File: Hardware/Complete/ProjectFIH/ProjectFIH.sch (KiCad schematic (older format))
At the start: 22 parts, among them J1 Conn_01x02_Male, J2 Heater, Q1 2N7002, Q2 2N7002, Q3 IRLZ44N, U1 LM158

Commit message: Added 24 -> 5 regulator
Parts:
- removed J1: Conn_01x02_Male, symbol Connector:Conn_01x02_Male
- added C?: 1000uF x 48V, symbol Device:CP
- added C? (x2): 2.2uF, symbol Device:C
- added C?: 10nF, symbol Device:C
- added C?: 1000uF x 10V, symbol Device:CP
- added D?: 10BQ060, symbol Device:D_Schottky
- added L?: 27uH 1A, symbol Device:L
- added U?: LM22675-5.0, symbol Fossa_library:LM22675-5.0
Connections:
- net +24V: now also C?.1, C?.1, U?.7 (Vin)
- net +5V: now also C?.1, C?.1, L?.2, U?.4 (FB)
- net GND: now also C?.2, C?.2, C?.2, C?.2, D?.2 (A), U?.6 (GND)
- new net: C?.1, D?.1 (K), L?.1, U?.8 (SW)
- new net: C?.2, U?.1 (Boot)
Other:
- note added: "Internal needs +5V regulator"
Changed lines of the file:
@@
 Wire Wire Line
 	900  1250 900  1500
-$Comp
-L Connector:Conn_01x02_Male J1
-U 1 1 5EFE5C5A
-P 1900 1100
-F 0 "J1" H 1962 1144 50  0000 L CNN
-F 1 "Conn_01x02_Male" H 1650 900 50  0000 L CNN
-F 2 "" H 1900 1100 50  0001 C CNN
-F 3 "~" H 1900 1100 50  0001 C CNN
-	1    1900 1100
-	-1   0    0    1
-$EndComp
 Wire Wire Line
 	1200 1500 1200 1400
-$Comp
-L power:GND #PWR011
-U 1 1 5EFEE96F
-P 1650 1150
-F 0 "#PWR011" H 1650 900 50  0001 C CNN
-F 1 "GND" H 1655 977 50  0000 C CNN
-F 2 "" H 1650 1150 50  0001 C CNN
-F 3 "" H 1650 1150 50  0001 C CNN
-	1    1650 1150
-	1    0    0    -1
-$EndComp
-$Comp
-L power:+5V #PWR010
-U 1 1 5EFEF193
-P 1650 950
-F 0 "#PWR010" H 1650 800 50  0001 C CNN
-F 1 "+5V" H 1665 1123 50  0000 C CNN
-F 2 "" H 1650 950 50  0001 C CNN
-F 3 "" H 1650 950 50  0001 C CNN
-	1    1650 950
-	1    0    0    -1
-$EndComp
-Wire Wire Line
-	1650 950  1650 1000
-Wire Wire Line
-	1650 1000 1700 1000
-Wire Wire Line
-	1700 1100 1650 1100
-Wire Wire Line
-	1650 1100 1650 1150
 Text Notes 2450 2000 0    50   ~ 0
 Uout = Uin * (1 + R3/R2 + R3/R1) - Vcc * R3/R1
@@
 Wire Wire Line
 	7600 2150 7600 2350
+$Comp
+L Device:CP C?
+U 1 1 5F0A2BBD
+P 8300 1350
+F 0 "C?" H 8300 1450 50  0000 L CNN
+F 1 "1000uF x 48V" H 8000 1250 50  0000 L CNN
+F 2 "" H 8338 1200 50  0001 C CNN
+F 3 "~" H 8300 1350 50  0001 C CNN
+	1    8300 1350
+	1    0    0    -1
+$EndComp
+$Comp
+L Device:C C?
+U 1 1 5F0A57D0
+P 8650 1350
+F 0 "C?" H 8650 1450 50  0000 L CNN
+F 1 "2.2uF" H 8600 1250 50  0000 L CNN
+F 2 "" H 8688 1200 50  0001 C CNN
+F 3 "~" H 8650 1350 50  0001 C CNN
+	1    8650 1350
+	1    0    0    -1
+$EndComp
+$Comp
+L Device:C C?
+U 1 1 5F0A5EBE
+P 9950 1350
+F 0 "C?" H 10065 1396 50  0000 L CNN
+F 1 "10nF" H 10065 1305 50  0000 L CNN
+F 2 "" H 9988 1200 50  0001 C CNN
+F 3 "~" H 9950 1350 50  0001 C CNN
+	1    9950 1350
+	0    1    1    0
+$EndComp
+$Comp
+L Device:C C?
+U 1 1 5F0A7836
+P 10750 1450
+F 0 "C?" H 10750 1550 50  0000 L CNN
+F 1 "2.2uF" H 10700 1350 50  0000 L CNN
+F 2 "" H 10788 1300 50  0001 C CNN
+F 3 "~" H 10750 1450 50  0001 C CNN
+	1    10750 1450
+	1    0    0    -1
+$EndComp
+$Comp
+L Device:CP C?
+U 1 1 5F0A7FA4
+P 11050 1450
+F 0 "C?" H 11100 1550 50  0000 L CNN
+F 1 "1000uF x 10V" H 10950 1350 50  0000 L CNN
+F 2 "" H 11088 1300 50  0001 C CNN
+F 3 "~" H 11050 1450 50  0001 C CNN
+	1    11050 1450
+	1    0    0    -1
+$EndComp
+$Comp
+L Device:L L?
+U 1 1 5F0A8920
+P 10450 1200
+F 0 "L?" V 10640 1200 50  0000 C CNN
+F 1 "27uH 1A" V 10549 1200 50  0000 C CNN
+F 2 "" H 10450 1200 50  0001 C CNN
+F 3 "~" H 10450 1200 50  0001 C CNN
+	1    10450 1200
+	0    -1   -1   0
+$EndComp
+$Comp
+L Device:D_Schottky D?
+U 1 1 5F0AEB09
+P 10200 1500
+F 0 "D?" V 10154 1580 50  0000 L CNN
+F 1 "10BQ060" V 10245 1580 50  0000 L CNN
+F 2 "" H 10200 1500 50  0001 C CNN
+F 3 "~" H 10200 1500 50  0001 C CNN
+	1    10200 1500
+	0    1    1    0
+$EndComp
+$Comp
+L Fossa_library:LM22675-5.0 U?
+U 1 1 5F0B9323
+P 9300 1150
+F 0 "U?" H 9300 1325 50  0000 C CNN
+F 1 "LM22675-5.0" H 9300 1234 50  0000 C CNN
+F 2 "" H 8450 1550 50  0001 C CNN
+F 3 "" H 8450 1550 50  0001 C CNN
+	1    9300 1150
+	1    0    0    -1
+$EndComp
+Wire Wire Line
+	8900 1200 8650 1200
+Wire Wire Line
+	8650 1200 8300 1200
+Connection ~ 8650 1200
+Wire Wire Line
+	8650 1500 8650 1750
+Wire Wire Line
+	8650 1750 9300 1750
+Wire Wire Line
+	9300 1750 9300 1650
+Wire Wire Line
+	8300 1500 8300 1750
+Wire Wire Line
+	8300 1750 8650 1750
+Connection ~ 8650 1750
+$Comp
+L power:+24V #PWR?
+U 1 1 5F0C36F2
+P 8300 1050
+F 0 "#PWR?" H 8300 900 50  0001 C CNN
+F 1 "+24V" H 8315 1223 50  0000 C CNN
+F 2 "" H 8300 1050 50  0001 C CNN
+F 3 "" H 8300 1050 50  0001 C CNN
+	1    8300 1050
+	1    0    0    -1
+$EndComp
+Wire Wire Line
+	8300 1050 8300 1200
+Connection ~ 8300 1200
+$Comp
+L power:GND #PWR?
+U 1 1 5F0C53FD
+P 9300 1850
+F 0 "#PWR?" H 9300 1600 50  0001 C CNN
+F 1 "GND" H 9305 1677 50  0000 C CNN
+F 2 "" H 9300 1850 50  0001 C CNN
+F 3 "" H 9300 1850 50  0001 C CNN
+	1    9300 1850
+	1    0    0    -1
+$EndComp
+Wire Wire Line
+	9300 1850 9300 1750
+Connection ~ 9300 1750
+Wire Wire Line
+	9700 1350 9800 1350
+Wire Wire Line
+	9700 1200 10100 1200
+Wire Wire Line
+	10100 1200 10100 1350
+Wire Wire Line
+	10100 1200 10200 1200
+Wire Wire Line
+	10200 1200 10200 1350
+Connection ~ 10100 1200
+Wire Wire Line
+	9300 1750 10200 1750
+Wire Wire Line
+	10200 1750 10200 1650
+Wire Wire Line
+	10300 1200 10200 1200
+Connection ~ 10200 1200
+Wire Wire Line
+	11050 1200 11050 1300
+Wire Wire Line
+	10750 1300 10750 1200
+Connection ~ 10750 1200
+Wire Wire Line
+	10750 1200 11050 1200
+Wire Wire Line
+	10750 1600 10750 1750
+Wire Wire Line
+	10750 1750 10200 1750
+Connection ~ 10200 1750
+Wire Wire Line
+	11050 1600 11050 1750
+Wire Wire Line
+	11050 1750 10750 1750
+Connection ~ 10750 1750
+Wire Wire Line
+	10600 1200 10750 1200
+Wire Wire Line
+	9700 1500 9750 1500
+Wire Wire Line
+	9750 1500 9750 950
+Wire Wire Line
+	9750 950  10750 950
+Wire Wire Line
+	10750 950  10750 1200
+$Comp
+L power:+5V #PWR?
+U 1 1 5F0F4926
+P 11050 1000
+F 0 "#PWR?" H 11050 850 50  0001 C CNN
+F 1 "+5V" H 11065 1173 50  0000 C CNN
+F 2 "" H 11050 1000 50  0001 C CNN
+F 3 "" H 11050 1000 50  0001 C CNN
+	1    11050 1000
+	1    0    0    -1
+$EndComp
+Wire Wire Line
+	11050 1000 11050 1200
+Connection ~ 11050 1200
+Text Notes 8850 850  0    50   ~ 0
+Internal needs +5V regulator
 $EndSCHEMATC

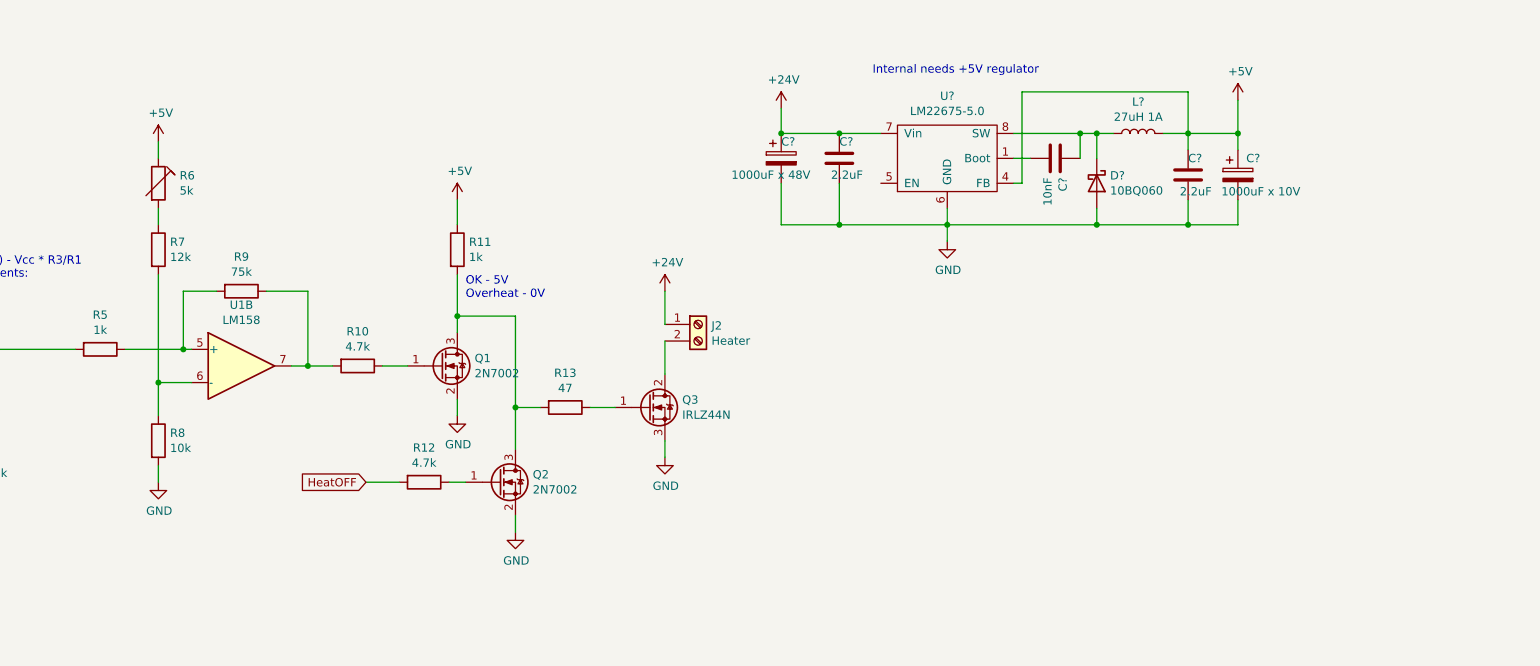
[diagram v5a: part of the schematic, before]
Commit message: Added payload regulator
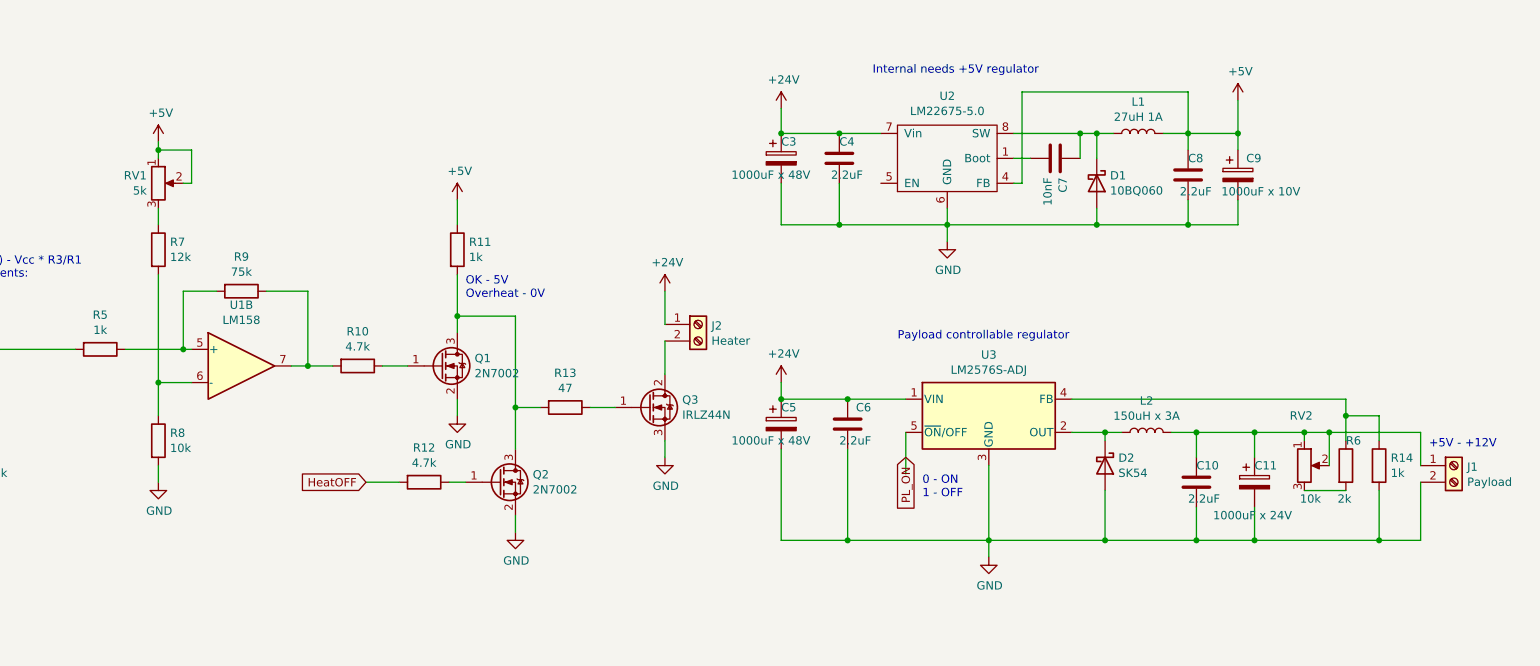
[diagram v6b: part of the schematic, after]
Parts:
- removed R6: 5k, symbol Device:RTRIM
- added C10, C6: 2.2uF, symbol Device:C
- added C11: 1000uF x 24V, symbol Device:CP
- added C5: 1000uF x 48V, symbol Device:CP
- added D2: SK54, symbol Device:D_Schottky
- added J1: Payload, symbol Connector:Screw_Terminal_01x02
- added L2: 150uH x 3A, symbol Device:L
- added R14: 1k, symbol Device:R
- added R6: 2k, symbol Device:R
- added RV1: 5k, symbol Device:R_POT
- added RV2: 10k, symbol Device:R_POT
- added U3: LM2576S-ADJ, Package_TO_SOT_SMD:TO-263-5_TabPin3, symbol Regulator_Switching:LM2576S-ADJ
- gave numbers to parts that had none: 8
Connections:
- net +24V: now also C5.1, C6.1, U3.1 (VIN)
- net +5V: now also RV1.1, RV1.2
- net GND: now also C10.2, C11.2, C5.2, C6.2, D2.2 (A), J1.2 (Pin_2), R14.2, U3.3 (GND)
- net at R7.1: now also RV1.3
- new net: D2.1 (K), L2.1, U3.2 (OUT)
- new net: R14.1, R6.1, U3.4 (FB)
- new net: C10.1, C11.1, J1.1 (Pin_1), L2.2, RV2.1, RV2.2
- new net: R6.2, RV2.3
- new net PL_ON: U3.5 (~ON~/OFF)
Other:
- note added: "+5V - +12V"
- note added: "0 - ON\n1 - OFF"
- note added: "Payload controllable regulator"

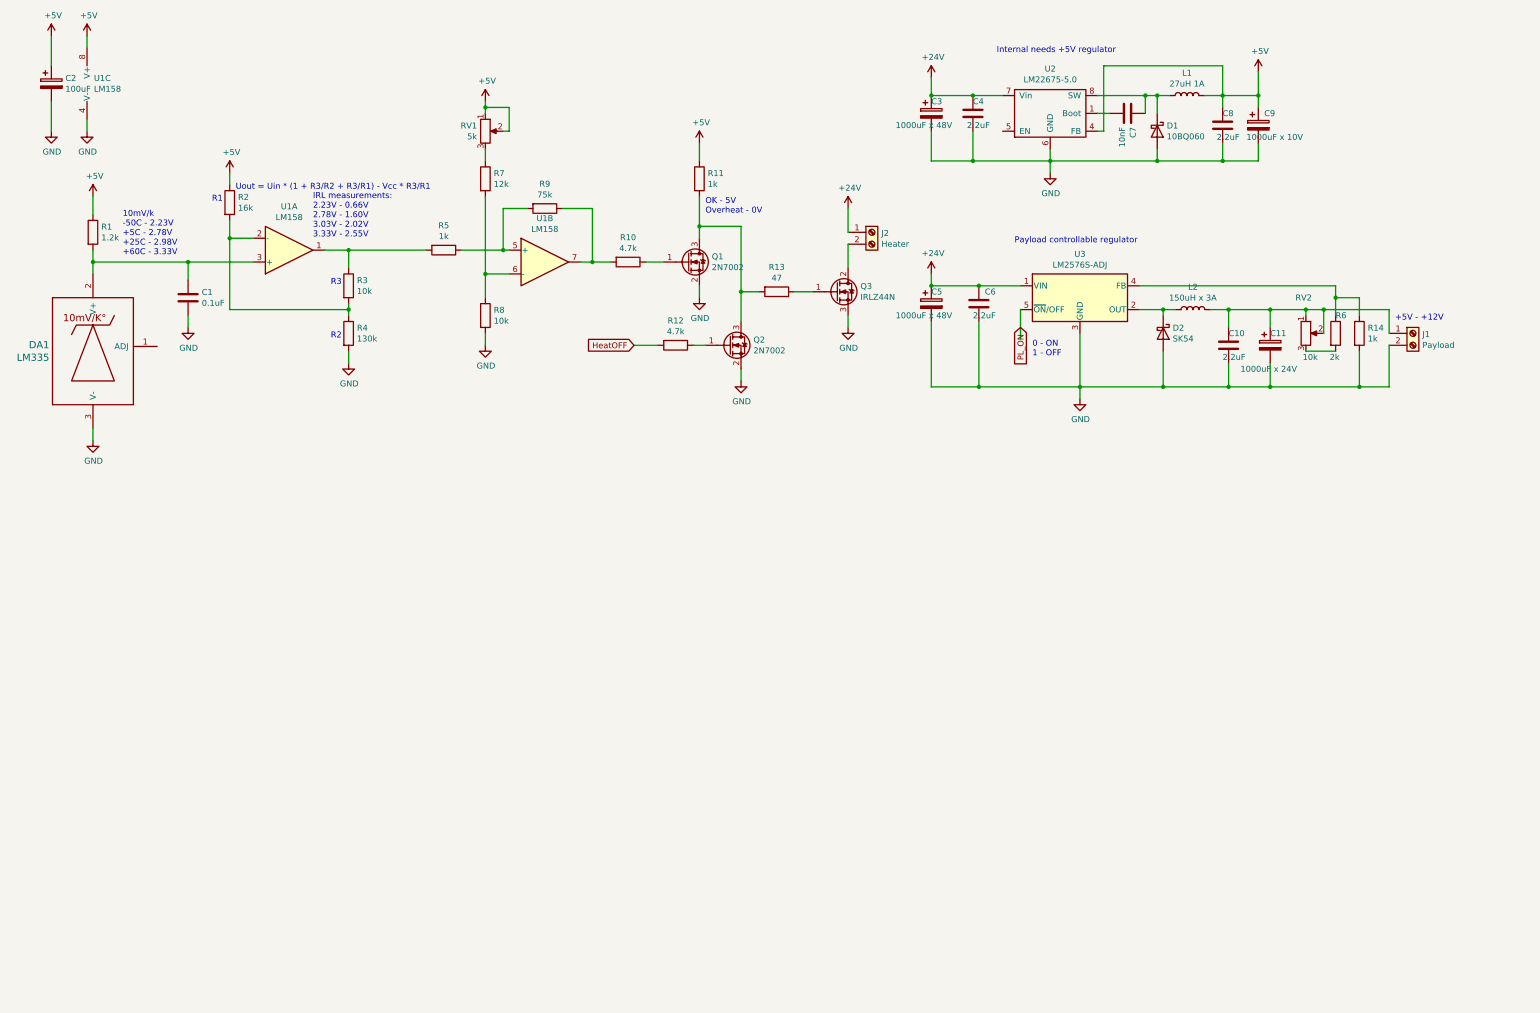
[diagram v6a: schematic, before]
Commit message: Added hardware watchdog
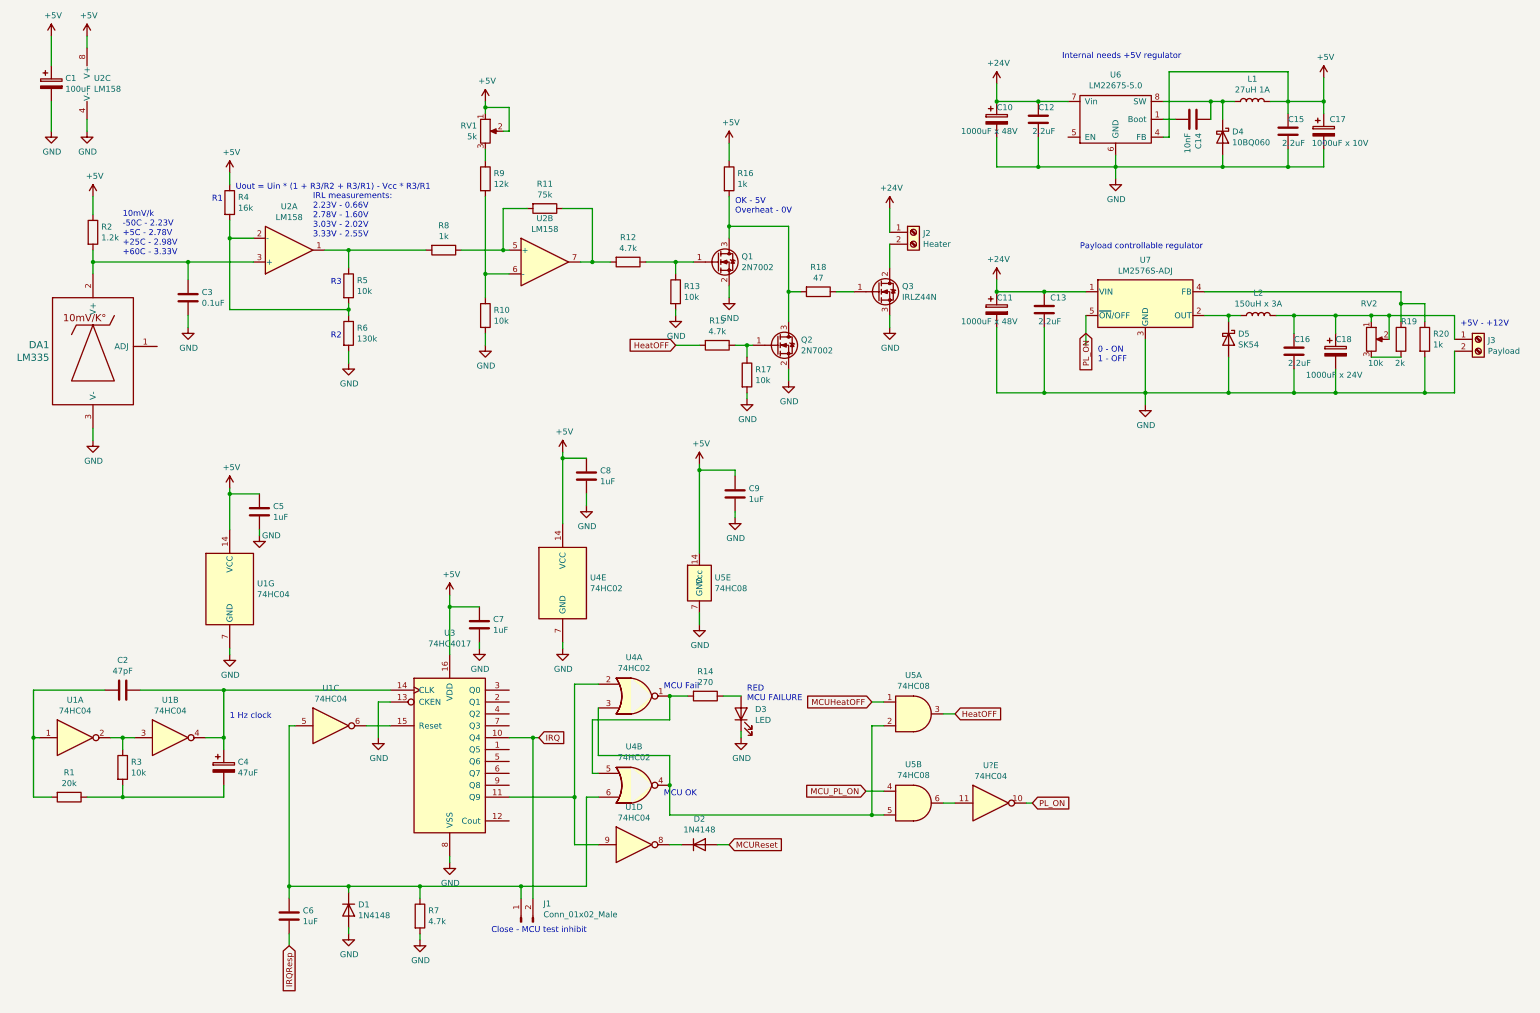
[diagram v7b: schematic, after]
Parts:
- added C2: 47pF, symbol Device:C
- added C4: 47uF, symbol Device:CP
- added C5, C6, C7, C8, C9: 1uF, symbol Device:C
- added D1, D2: 1N4148, Diode_THT:D_DO-35_SOD27_P7.62mm_Horizontal, symbol Diode:1N4148
- added D3: LED, symbol Device:LED
- added J1: Conn_01x02_Male, symbol Connector:Conn_01x02_Male
- added R1: 20k, symbol Device:R
- added R13, R17, R3: 10k, symbol Device:R
- added R14: 270, symbol Device:R
- added R7: 4.7k, symbol Device:R
- added U1, U?: 74HC04, symbol 74xx:74HC04
- added U3: 74HC4017, symbol 4xxx:4017
- added U4: 74HC02, symbol 74xx:74HC02
- added U5: 74HC08, symbol Fossa_library:74HC08
- renumbered C2 to C1, C3 to C10, C5 to C11, C4 to C12, C6 to C13, C7 to C14, C8 to C15, C10 to C16, C9 to C17, C11 to C18, C1 to C3, D1 to D4, D2 to D5, J1 to J3, R8 to R10, R9 to R11, R10 to R12, R12 to R15, R11 to R16, R13 to R18, R6 to R19, R1 to R2, R14 to R20, R2 to R4, R3 to R5, R4 to R6, R5 to R8, R7 to R9, U1 to U2, U2 to U6, U3 to U7
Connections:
- net +5V: now also C5.1, C7.1, C8.1, C9.1, U1.14 (VCC), U3.16 (VDD), U4.14 (VCC), U5.14 (Vcc)
- net GND: now also C5.2, C7.2, C8.2, C9.2, D1.2 (A), D3.1 (K), R13.2, R17.2, R7.2, U1.7 (GND), U3.13 (CKEN), U3.8 (VSS), U4.7 (GND), U5.7 (GND)
- net HeatOFF: now also U5.3
- net PL_ON: now also U?.10
- net at Q2.1 (G), R15.1: now also R17.1
- net at Q1.1 (G), R12.1: now also R13.1
- new net: C2.2, R1.2, U1.1
- new net: R3.1, U1.2, U1.3
- new net: C2.1, C4.1, U1.4, U3.14 (CLK)
- new net: C4.2, R1.1, R3.2
- new net: D3.2 (A), R14.1
- new net: R14.2, U4.1, U4.5
- new net: U1.9, U3.11 (Q9), U4.2
- new net: U1.6, U3.15 (Reset)
- new net: C6.1, D1.1 (K), J1.1 (Pin_1), R7.1, U1.5, U4.6
- new net: U4.3, U4.4, U5.2, U5.5
- new net: U5.6, U?.11
- new net: D2.1 (K), U1.8
- new net IRQ: J1.2 (Pin_2), U3.10 (Q4)
- new net IRQResp: C6.2
- new net MCUHeatOFF: U5.1
- new net MCUReset: D2.2 (A)
- new net MCU_PL_ON: U5.4
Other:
- note added: "1 Hz clock"
- note added: "Close - MCU test inhibit"
- note added: "MCU Fail"
- note added: "MCU OK"
- note added: "RED\nMCU FAILURE"
- moved on the sheet: C10, C11, C12, C13, C14, C15, C16, C17, C18, D4, D5, J2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
